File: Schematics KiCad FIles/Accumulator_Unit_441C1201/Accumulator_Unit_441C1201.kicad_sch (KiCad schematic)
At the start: 31 parts, among them J1 Edge

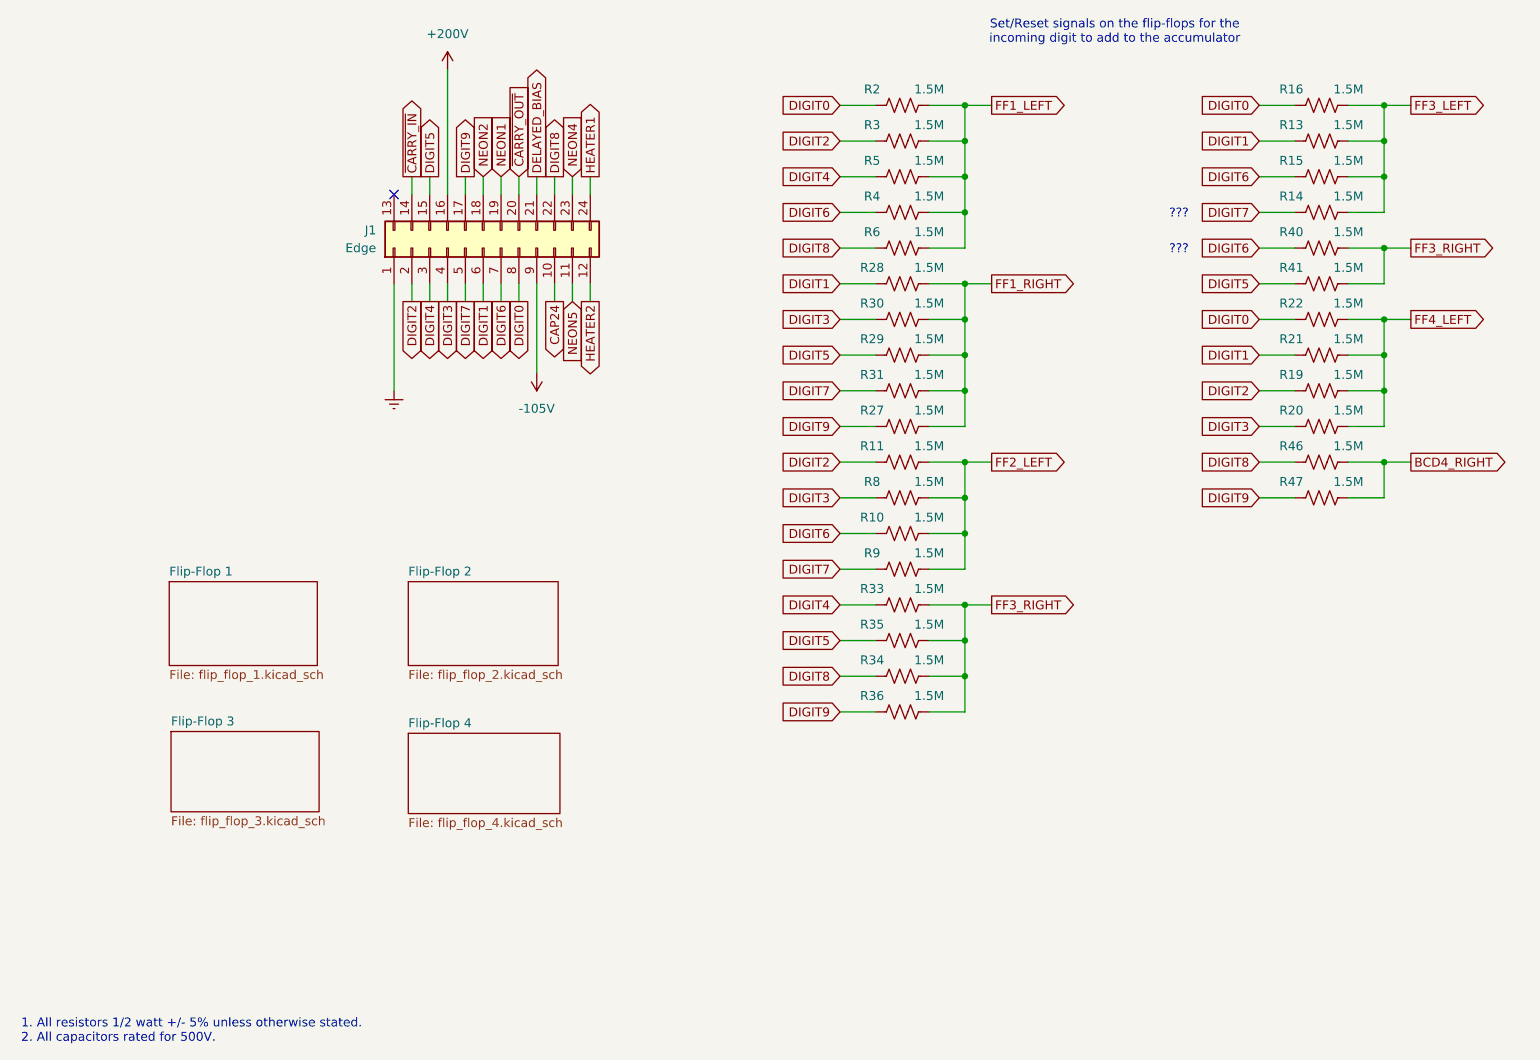
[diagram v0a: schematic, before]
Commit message: Fix component designators on accumulator schematics
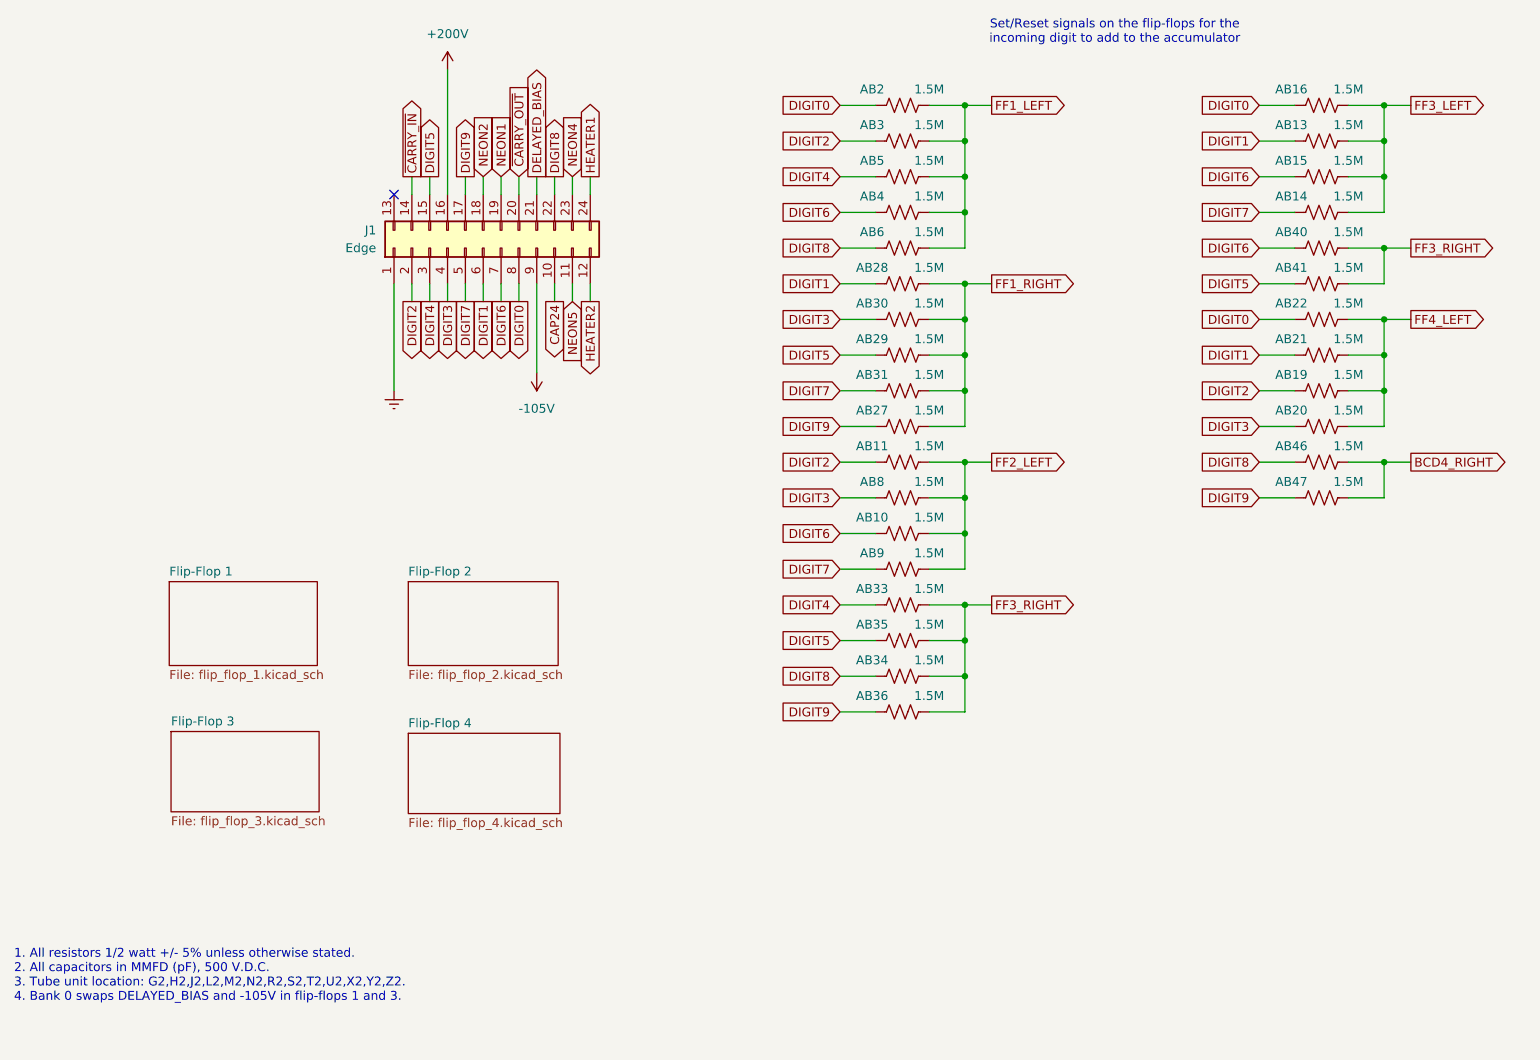
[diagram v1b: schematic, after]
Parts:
- renumbered R10 to AB10, R11 to AB11, R13 to AB13, R14 to AB14, R15 to AB15, R16 to AB16, R19 to AB19, R2 to AB2, R20 to AB20, R21 to AB21, R22 to AB22, R27 to AB27, R28 to AB28, R29 to AB29, R3 to AB3, R30 to AB30, R31 to AB31, R33 to AB33, R34 to AB34, R35 to AB35, R36 to AB36, R4 to AB4, R40 to AB40, R41 to AB41, R46 to AB46, R47 to AB47, R5 to AB5, R6 to AB6, R8 to AB8, R9 to AB9
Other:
- note added: "1. All resistors 1/2 watt +/- 5% unless otherwise stated. 2. All capacitors in MMFD (pF), 500 V.D.C. 3. Tube unit location: G2,H2,J2,L2,M2,N2,R2,S2,T2,U2,X2,Y2,Z2. 4. Bank 0 swaps DELAYED_BIAS and -105V in flip-flops 1 and 3."
- note removed: "1. All resistors 1/2 watt +/- 5% unless otherwise stated. 2. All capacitors rated for 500V."
- note removed: "???"
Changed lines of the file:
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@@
 		(title "Compu-Tronic Accumulator Unit Schematic")
 		(date "10-23-1958")
+		(comment 2 "For wiring diagram see 441E1302")
 	)
 	(junction
@@
 		)
 	)
-	(text "1. All resistors 1/2 watt +/- 5% unless otherwise stated.\n2. All capacitors rated for 500V."
+	(text "1. All resistors 1/2 watt +/- 5% unless otherwise stated.\n2. All capacitors in MMFD (pF), 500 V.D.C.\n3. Tube unit location: G2,H2,J2,L2,M2,N2,R2,S2,T2,U2,X2,Y2,Z2.\n4. Bank 0 swaps DELAYED_BIAS and -105V in flip-flops 1 and 3."
 		(exclude_from_sim no)
-		(at 32.004 178.816 0)
+		(at 30.988 170.942 0)
 		(effects
 			(font
@@
 		)
 	)
-	(text "???"
-		(exclude_from_sim no)
-		(at 196.85 67.564 0)
-		(effects
-			(font
-				(size 1.27 1.27)
-			)
-		)
-	)
-	(text "???"
-		(exclude_from_sim no)
-		(at 196.85 62.484 0)
-		(effects
-			(font
-				(size 1.27 1.27)
-			)
-		)
-	)
 	(text "Set/Reset signals on the flip-flops for the\nincoming digit to add to the accumulator"
 		(exclude_from_sim no)
@@
 		(on_board yes)
 		(dnp no)
-		(property "Reference" "R31"
+		(property "Reference" "AB31"
 			(at 153.162 85.344 90)
 			(effects
@@
 			(project "Accumulator_Unit_441C1201"
 				(path "/519d7692-6bf3-45ab-bd58-713783b63e8a"
-					(reference "R31")
+					(reference "AB31")
 					(unit 1)
 				)
@@
 		(on_board yes)
 		(dnp no)
-		(property "Reference" "R40"
+		(property "Reference" "AB40"
 			(at 212.852 65.024 90)
 			(effects
@@
 			(project "Accumulator_Unit_441C1201"
 				(path "/519d7692-6bf3-45ab-bd58-713783b63e8a"
-					(reference "R40")
+					(reference "AB40")
 					(unit 1)
 				)
@@
 		(on_board yes)
 		(dnp no)
-		(property "Reference" "R41"
+		(property "Reference" "AB41"
 			(at 212.852 70.104 90)
 			(effects
@@
 			(project "Accumulator_Unit_441C1201"
 				(path "/519d7692-6bf3-45ab-bd58-713783b63e8a"
-					(reference "R41")
+					(reference "AB41")
 					(unit 1)
 				)
@@
 		(on_board yes)
 		(dnp no)
-		(property "Reference" "R20"
+		(property "Reference" "AB20"
 			(at 212.852 90.424 90)
 			(effects
@@
 			(project "Accumulator_Unit_441C1201"
 				(path "/519d7692-6bf3-45ab-bd58-713783b63e8a"
-					(reference "R20")
+					(reference "AB20")
 					(unit 1)
 				)
@@
 		(on_board yes)
 		(dnp no)
-		(property "Reference" "R16"
+		(property "Reference" "AB16"
 			(at 212.852 44.704 90)
 			(effects
@@
 			(project "Accumulator_Unit_441C1201"
 				(path "/519d7692-6bf3-45ab-bd58-713783b63e8a"
-					(reference "R16")
+					(reference "AB16")
 					(unit 1)
 				)
@@
 		(on_board yes)
 		(dnp no)
-		(property "Reference" "R9"
+		(property "Reference" "AB9"
 			(at 153.162 110.744 90)
 			(effects
@@
 			(project "Accumulator_Unit_441C1201"
 				(path "/519d7692-6bf3-45ab-bd58-713783b63e8a"
-					(reference "R9")
+					(reference "AB9")
 					(unit 1)
 				)
@@
 		(on_board yes)
 		(dnp no)
-		(property "Reference" "R3"
+		(property "Reference" "AB3"
 			(at 153.162 49.784 90)
 			(effects
@@
 			(project "Accumulator_Unit_441C1201"
 				(path "/519d7692-6bf3-45ab-bd58-713783b63e8a"
-					(reference "R3")
+					(reference "AB3")
 					(unit 1)
 				)
@@
 		(on_board yes)
 		(dnp no)
-		(property "Reference" "R34"
+		(property "Reference" "AB34"
 			(at 153.162 125.984 90)
 			(effects
@@
 			(project "Accumulator_Unit_441C1201"
 				(path "/519d7692-6bf3-45ab-bd58-713783b63e8a"
-					(reference "R34")
+					(reference "AB34")
 					(unit 1)
 				)
@@
 		(on_board yes)
 		(dnp no)
-		(property "Reference" "R33"
+		(property "Reference" "AB33"
 			(at 153.162 115.824 90)
 			(effects
@@
 			(project "Accumulator_Unit_441C1201"
 				(path "/519d7692-6bf3-45ab-bd58-713783b63e8a"
-					(reference "R33")
+					(reference "AB33")
 					(unit 1)
 				)
@@
 		(on_board yes)
 		(dnp no)
-		(property "Reference" "R8"
+		(property "Reference" "AB8"
 			(at 153.162 100.584 90)
 			(effects
@@
 			(project "Accumulator_Unit_441C1201"
 				(path "/519d7692-6bf3-45ab-bd58-713783b63e8a"
-					(reference "R8")
+					(reference "AB8")
 					(unit 1)
 				)
@@
 		(on_board yes)
 		(dnp no)
-		(property "Reference" "R47"
+		(property "Reference" "AB47"
 			(at 212.852 100.584 90)
 			(effects
@@
 			(project "Accumulator_Unit_441C1201"
 				(path "/519d7692-6bf3-45ab-bd58-713783b63e8a"
-					(reference "R47")
+					(reference "AB47")
 					(unit 1)
 				)
@@
 		(on_board yes)
 		(dnp no)
-		(property "Reference" "R22"
+		(property "Reference" "AB22"
 			(at 212.852 75.184 90)
 			(effects
@@
 			(project "Accumulator_Unit_441C1201"
 				(path "/519d7692-6bf3-45ab-bd58-713783b63e8a"
-					(reference "R22")
+					(reference "AB22")
 					(unit 1)
 				)
@@
 		(on_board yes)
 		(dnp no)
-		(property "Reference" "R29"
+		(property "Reference" "AB29"
 			(at 153.162 80.264 90)
 			(effects
@@
 			(project "Accumulator_Unit_441C1201"
 				(path "/519d7692-6bf3-45ab-bd58-713783b63e8a"
-					(reference "R29")
+					(reference "AB29")
 					(unit 1)
 				)
@@
 		(on_board yes)
 		(dnp no)
-		(property "Reference" "R2"
+		(property "Reference" "AB2"
 			(at 153.162 44.704 90)
 			(effects
@@
 			(project ""
 				(path "/519d7692-6bf3-45ab-bd58-713783b63e8a"
-					(reference "R2")
+					(reference "AB2")
 					(unit 1)
 				)
@@
 		(on_board yes)
 		(dnp no)
-		(property "Reference" "R14"
+		(property "Reference" "AB14"
 			(at 212.852 59.944 90)
 			(effects
@@
 			(project "Accumulator_Unit_441C1201"
 				(path "/519d7692-6bf3-45ab-bd58-713783b63e8a"
-					(reference "R14")
+					(reference "AB14")
 					(unit 1)
 				)
@@
 		(on_board yes)
 		(dnp no)
-		(property "Reference" "R46"
+		(property "Reference" "AB46"
 			(at 212.852 95.504 90)
 			(effects
@@
 			(project "Accumulator_Unit_441C1201"
 				(path "/519d7692-6bf3-45ab-bd58-713783b63e8a"
-					(reference "R46")
+					(reference "AB46")
 					(unit 1)
 				)
@@
 		(on_board yes)
 		(dnp no)
-		(property "Reference" "R5"
+		(property "Reference" "AB5"
 			(at 153.162 54.864 90)
 			(effects
@@
 			(project "Accumulator_Unit_441C1201"
 				(path "/519d7692-6bf3-45ab-bd58-713783b63e8a"
-					(reference "R5")
+					(reference "AB5")
 					(unit 1)
 				)
@@
 		(on_board yes)
 		(dnp no)
-		(property "Reference" "R35"
+		(property "Reference" "AB35"
 			(at 153.162 120.904 90)
 			(effects
@@
 			(project "Accumulator_Unit_441C1201"
 				(path "/519d7692-6bf3-45ab-bd58-713783b63e8a"
-					(reference "R35")
+					(reference "AB35")
 					(unit 1)
 				)
@@
 		(on_board yes)
 		(dnp no)
-		(property "Reference" "R15"
+		(property "Reference" "AB15"
 			(at 212.852 54.864 90)
 			(effects
@@
 			(project "Accumulator_Unit_441C1201"
 				(path "/519d7692-6bf3-45ab-bd58-713783b63e8a"
-					(reference "R15")
+					(reference "AB15")
 					(unit 1)
 				)
@@
 		(on_board yes)
 		(dnp no)
-		(property "Reference" "R28"
+		(property "Reference" "AB28"
 			(at 153.162 70.104 90)
 			(effects
@@
 			(project "Accumulator_Unit_441C1201"
 				(path "/519d7692-6bf3-45ab-bd58-713783b63e8a"
-					(reference "R28")
+					(reference "AB28")
 					(unit 1)
 				)
@@
 		(on_board yes)
 		(dnp no)
-		(property "Reference" "R4"
+		(property "Reference" "AB4"
 			(at 153.162 59.944 90)
 			(effects
@@
 			(project "Accumulator_Unit_441C1201"
 				(path "/519d7692-6bf3-45ab-bd58-713783b63e8a"
-					(reference "R4")
+					(reference "AB4")
 					(unit 1)
 				)
@@
 		(on_board yes)
 		(dnp no)
-		(property "Reference" "R10"
+		(property "Reference" "AB10"
 			(at 153.162 105.664 90)
 			(effects
@@
 			(project "Accumulator_Unit_441C1201"
 				(path "/519d7692-6bf3-45ab-bd58-713783b63e8a"
-					(reference "R10")
+					(reference "AB10")
 					(unit 1)
 				)
@@
 		(on_board yes)
 		(dnp no)
-		(property "Reference" "R21"
+		(property "Reference" "AB21"
 			(at 212.852 80.264 90)
 			(effects
@@
 			(project "Accumulator_Unit_441C1201"
 				(path "/519d7692-6bf3-45ab-bd58-713783b63e8a"
-					(reference "R21")
+					(reference "AB21")
 					(unit 1)
 				)
@@
 		(on_board yes)
 		(dnp no)
-		(property "Reference" "R13"
+		(property "Reference" "AB13"
 			(at 212.852 49.784 90)
 			(effects
@@
 			(project "Accumulator_Unit_441C1201"
 				(path "/519d7692-6bf3-45ab-bd58-713783b63e8a"
-					(reference "R13")
+					(reference "AB13")
 					(unit 1)
 				)
@@
 		(on_board yes)
 		(dnp no)
-		(property "Reference" "R11"
+		(property "Reference" "AB11"
 			(at 153.162 95.504 90)
 			(effects
@@
 			(project "Accumulator_Unit_441C1201"
 				(path "/519d7692-6bf3-45ab-bd58-713783b63e8a"
-					(reference "R11")
+					(reference "AB11")
 					(unit 1)
 				)
@@
 		(on_board yes)
 		(dnp no)
-		(property "Reference" "R19"
+		(property "Reference" "AB19"
 			(at 212.852 85.344 90)
 			(effects
@@
 			(project "Accumulator_Unit_441C1201"
 				(path "/519d7692-6bf3-45ab-bd58-713783b63e8a"
-					(reference "R19")
+					(reference "AB19")
 					(unit 1)
 				)
@@
 		(on_board yes)
 		(dnp no)
-		(property "Reference" "R6"
+		(property "Reference" "AB6"
 			(at 153.162 65.024 90)
 			(effects
@@
 			(project "Accumulator_Unit_441C1201"
 				(path "/519d7692-6bf3-45ab-bd58-713783b63e8a"
-					(reference "R6")
+					(reference "AB6")
 					(unit 1)
 				)
@@
 		(on_board yes)
 		(dnp no)
-		(property "Reference" "R36"
+		(property "Reference" "AB36"
 			(at 153.162 131.064 90)
 			(effects
@@
 			(project "Accumulator_Unit_441C1201"
 				(path "/519d7692-6bf3-45ab-bd58-713783b63e8a"
-					(reference "R36")
+					(reference "AB36")
 					(unit 1)
 				)
@@
 		(on_board yes)
 		(dnp no)
-		(property "Reference" "R27"
+		(property "Reference" "AB27"
 			(at 153.162 90.424 90)
 			(effects
@@
 			(project "Accumulator_Unit_441C1201"
 				(path "/519d7692-6bf3-45ab-bd58-713783b63e8a"
-					(reference "R27")
+					(reference "AB27")
 					(unit 1)
 				)
@@
 		(on_board yes)
 		(dnp no)
-		(property "Reference" "R30"
+		(property "Reference" "AB30"
 			(at 153.162 75.184 90)
 			(effects
@@
 			(project "Accumulator_Unit_441C1201"
 				(path "/519d7692-6bf3-45ab-bd58-713783b63e8a"
-					(reference "R30")
+					(reference "AB30")
 					(unit 1)
 				)
